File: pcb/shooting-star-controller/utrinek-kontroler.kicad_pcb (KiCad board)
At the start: 2 copper layers, 48.3 x 48.3 mm, 11 parts, among them IC1 ATTINY841-SSU, J1 RJ45, P1 CONN_01X05, P2 CONN_01X02, P3 CONN_01X06

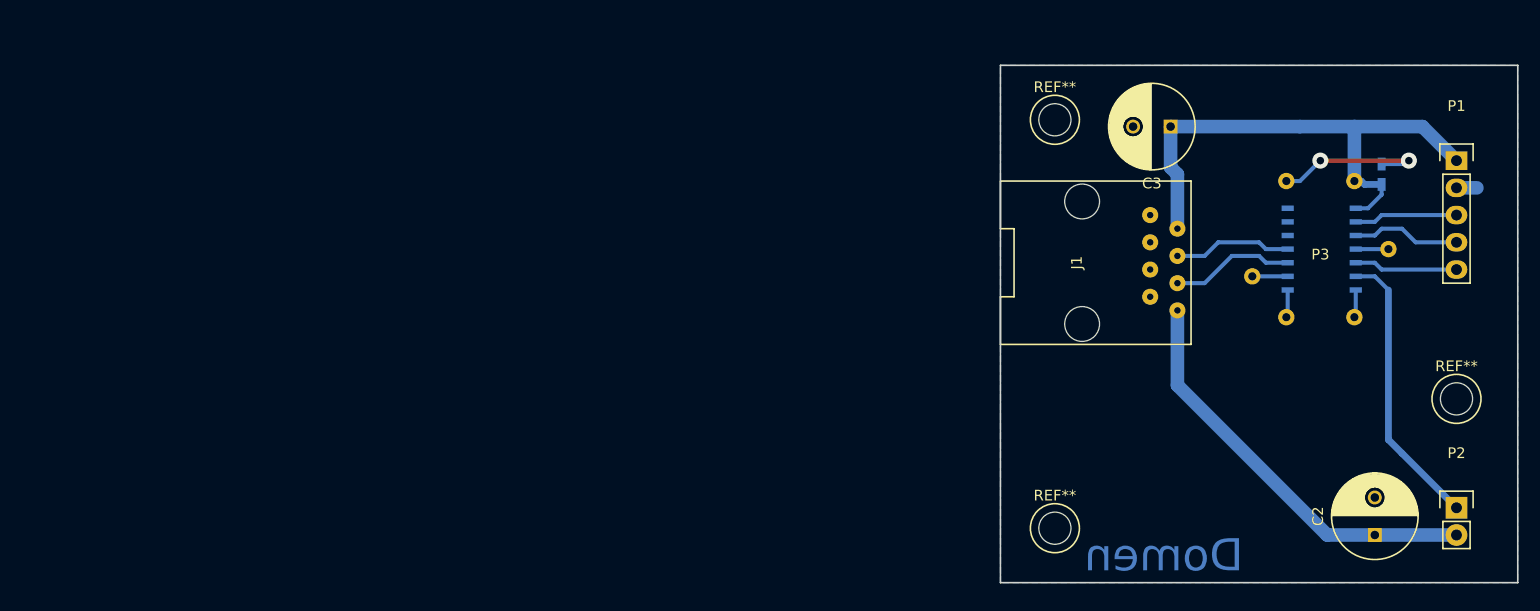
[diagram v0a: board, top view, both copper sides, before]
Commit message: Double sided pcbs
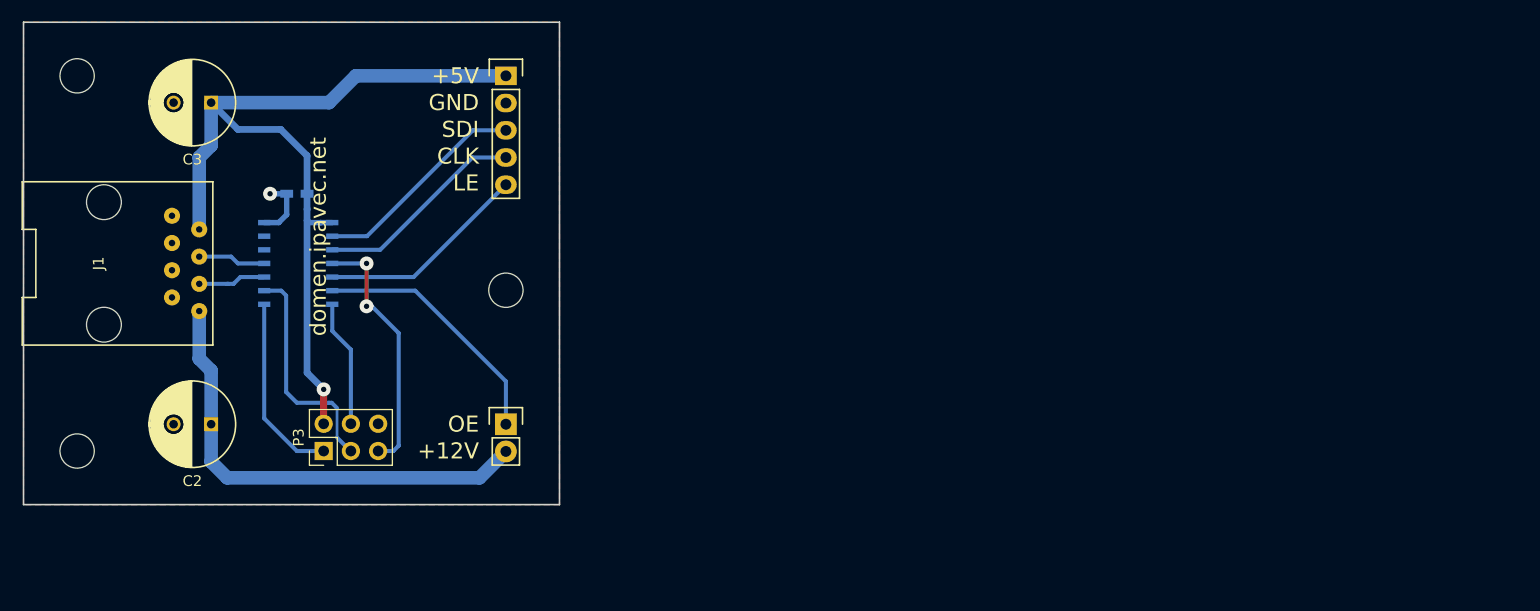
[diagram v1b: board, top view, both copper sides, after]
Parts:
- removed the REF** at (233.7, 127.6)
- removed the REF** at (196.2, 101.6)
- removed the REF** at (196.2, 139.7)
- added REF**: MountingHole_3.2mm_M3, Mounting_Holes:MountingHole_3.2mm_M3, F.Cu at (105.0, 97.5)
- added REF**: MountingHole_3.2mm_M3, Mounting_Holes:MountingHole_3.2mm_M3, F.Cu at (105.0, 132.5)
- added REF**: MountingHole_3.2mm_M3, Mounting_Holes:MountingHole_3.2mm_M3, F.Cu at (145.0, 117.5)
- P3: footprint attiny841-spi:ATTINY841-SPI -> Pin_Headers:Pin_Header_Straight_2x03_Pitch2.54mm
- moved C2 109.1 mm to (117.5, 130.0), turned to 180 degrees
- moved C1 101.2 mm to (125.5, 108.5), turned to 180 degrees
- moved IC1 95.5 mm to (125.5, 115.0)
- moved P3 94.9 mm to (128.0, 132.5), turned to 90 degrees
- moved J1 91.3 mm to (107.5, 115.0)
- moved C3 89.5 mm to (117.5, 100.0)
- moved P1 89.0 mm to (145.0, 97.5)
- moved P2 89.0 mm to (145.0, 130.0)
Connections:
- IC1 pad 12: Net-(IC1-Pad12) -> (no net)
- IC1 pad 13: Net-(IC1-Pad13) -> (no net)
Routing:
- net +5V: track 49.4 -> 80.1 mm, vias 0 -> 1
- net AVR_RESET: track 3.05 -> 23.9 mm, vias 0 -> 2
- net AVR_SCK: track 3.30 -> 21.2 mm
- net AVR_MISO: track 2.59 -> 17.5 mm
- net GND: track 16.8 -> 5.90 mm, vias 2 -> 1
- net LED_DATA: track 9.66 -> 20.3 mm
- net LED_LATCH: track 9.66 -> 19.8 mm
- net LED_CLOCK: track 10.2 -> 19.8 mm
- net AVR_MOSI: track 2.59 -> 11.9 mm
- net XCK: track 11.6 -> 6.42 mm
- net +12V: track 38.8 -> 43.7 mm
- net RXD: track 11.1 -> 6.33 mm
- net LED_ENABLE: track 26.5 -> 23.7 mm
- added copper zone on F.Cu, net GND
- removed copper zone on B.Cu, net GND
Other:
- board size 48.3 x 48.3 mm -> 50 x 45 mm
- net class Default: clearance 0.381 -> 0.254; trace_width 0.381 -> 0.254; via_dia 1.5 -> 1.3; via_drill 0.7 -> 0.5
- rule trace_clearance: 0.381 -> 0.254
- board text added: "+12V"
- board text added: "+5V"
- board text added: "CLK"
- board text added: "GND"
- board text added: "LE"
- board text added: "OE"
- board text added: "SDI"
- board text added: "domen.ipavec.net"
- board text removed: "Domen"
